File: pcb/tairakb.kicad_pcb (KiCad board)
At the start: 2 copper layers, 144 x 116 mm, 79 parts, among them SW1 SW_Push, SW10 SW_Push, SW11 SW_Push, SW12 SW_Push, SW13 SW_Push, SW14 SW_Push, SW15 SW_Push, SW16 SW_Push, SW17 SW_Push, SW18 SW_Push, SW19 SW_Push, SW2 SW_Push, SW20 SW_Push, SW20-1 SW_Push, SW21 SW_Push, SW22 SW_Push, SW23 SW_Push, SW24 SW_Push, SW25 SW_Push, SW26 SW_Push, SW27 SW_Push, SW28 SW_Push, SW29 SW_Push, SW3 SW_Push, SW30 SW_Push, SW31 SW_Push, SW32 SW_Push, SW33 SW_Push, SW4 SW_Push, SW5 SW_Push, SW6 SW_Push, SW7 SW_Push, SW8 SW_Push, SW9 SW_Push, U3 nice!nano

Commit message: Add traces routed by hand
Previously the diodes were connected from the columns to the switches.
Both the ErgoDash and the Corne have them behind the switches connected
to the rows. Since I positioned the diodes on the PCB like they are in
the ErgoDash and Corne, the routing was much more difficult than intended.

This moves the diodes behind the switches and also moves them around a
bit on the PCB. This allowed me to hand route all traces easily, so this
time no autorouter has been involved.

The via count is rather large (156). I opted to rather have ONE trace
and then interconnect each component with vias itself. An alternative
could be to run traces for rows and columns on both layers, but then
there still would be a lot of conflicting paths requiring vias anyway.

I also removed both GND zones. There is nothing on the board that needs
ground except the nice!nano and the battery and I didn't want to start
adding complicated routing just to get GND zones on the whole board. I
left one GND zone in the nice!nano area since it seems reasonable there.
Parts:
- moved D32 20.9 mm to (199.6, 109.6), turned to 330 degrees
- moved D30 16.6 mm to (196.0, 144.4)
- moved D33 16.6 mm to (211.6, 153.4)
- moved D25 16.6 mm to (180.3, 135.5)
- moved D31 12.0 mm to (198.7, 111.1), turned to 330 degrees
- turned D1 to 270 degrees
- turned D10 to 270 degrees
- turned D11 to 270 degrees
- turned D12 to 270 degrees
- turned D13 to 270 degrees
- turned D14 to 270 degrees
- turned D15 to 270 degrees
- turned D16 to 270 degrees
- turned D17 to 270 degrees
- turned D18 to 270 degrees
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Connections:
- D1 pad 1: Net-(D1-Pad1) -> /row0
- D1 pad 2: /col0 -> Net-(D1-Pad2)
- D10 pad 1: Net-(D10-Pad1) -> /row4
- D10 pad 2: /col1 -> Net-(D10-Pad2)
- D11 pad 1: Net-(D11-Pad1) -> /row0
- D11 pad 2: /col2 -> Net-(D11-Pad2)
- D12 pad 1: Net-(D12-Pad1) -> /row1
- D12 pad 2: /col2 -> Net-(D12-Pad2)
- D13 pad 1: Net-(D13-Pad1) -> /row2
- D13 pad 2: /col2 -> Net-(D13-Pad2)
- D14 pad 1: Net-(D14-Pad1) -> /row3
- D14 pad 2: /col2 -> Net-(D14-Pad2)
- D15 pad 1: Net-(D15-Pad1) -> /row4
- D15 pad 2: /col2 -> Net-(D15-Pad2)
- D16 pad 1: Net-(D16-Pad1) -> /row0
- D16 pad 2: /col3 -> Net-(D16-Pad2)
- D17 pad 1: Net-(D17-Pad1) -> /row1
- D17 pad 2: /col3 -> Net-(D17-Pad2)
- D18 pad 1: Net-(D18-Pad1) -> /row2
- D18 pad 2: /col3 -> Net-(D18-Pad2)
- D19 pad 1: Net-(D19-Pad1) -> /row3
- D19 pad 2: /col3 -> Net-(D19-Pad2)
- D2 pad 1: Net-(D2-Pad1) -> /row1
- D2 pad 2: /col0 -> Net-(D2-Pad2)
- D20 pad 1: Net-(D20-Pad1) -> /row4
- D20 pad 2: /col3 -> Net-(D20-Pad2)
- D21 pad 1: Net-(D21-Pad1) -> /row0
- D21 pad 2: /col4 -> Net-(D21-Pad2)
- D22 pad 1: Net-(D22-Pad1) -> /row1
- D22 pad 2: /col4 -> Net-(D22-Pad2)
- D23 pad 1: Net-(D23-Pad1) -> /row2
- D23 pad 2: /col4 -> Net-(D23-Pad2)
- D24 pad 1: Net-(D24-Pad1) -> /row3
- D24 pad 2: /col4 -> Net-(D24-Pad2)
- D25 pad 1: Net-(D25-Pad1) -> /row4
- D25 pad 2: /col4 -> Net-(D25-Pad2)
- D26 pad 1: Net-(D26-Pad1) -> /row0
- D26 pad 2: /col5 -> Net-(D26-Pad2)
- D27 pad 1: Net-(D27-Pad1) -> /row1
- D27 pad 2: /col5 -> Net-(D27-Pad2)
- D28 pad 1: Net-(D28-Pad1) -> /row2
- D28 pad 2: /col5 -> Net-(D28-Pad2)
- D29 pad 1: Net-(D29-Pad1) -> /row3
- D29 pad 2: /col5 -> Net-(D29-Pad2)
- D3 pad 1: Net-(D3-Pad1) -> /row2
- D3 pad 2: /col0 -> Net-(D3-Pad2)
- D30 pad 1: Net-(D30-Pad1) -> /row4
- D30 pad 2: /col5 -> Net-(D30-Pad2)
- D31 pad 1: Net-(D31-Pad1) -> /row2
- D31 pad 2: /col6 -> Net-(D31-Pad2)
- D32 pad 1: Net-(D32-Pad1) -> /row3
- D32 pad 2: /col6 -> Net-(D32-Pad2)
- D33 pad 1: Net-(D33-Pad1) -> /row4
- D33 pad 2: /col6 -> Net-(D33-Pad2)
- D4 pad 1: Net-(D4-Pad1) -> /row3
- D4 pad 2: /col0 -> Net-(D4-Pad2)
- D5 pad 1: Net-(D5-Pad1) -> /row4
- D5 pad 2: /col0 -> Net-(D5-Pad2)
- D6 pad 1: Net-(D6-Pad1) -> /row0
- D6 pad 2: /col1 -> Net-(D6-Pad2)
- D7 pad 1: Net-(D7-Pad1) -> /row1
- D7 pad 2: /col1 -> Net-(D7-Pad2)
- D8 pad 1: Net-(D8-Pad1) -> /row2
- D8 pad 2: /col1 -> Net-(D8-Pad2)
- D9 pad 1: Net-(D9-Pad1) -> /row3
- D9 pad 2: /col1 -> Net-(D9-Pad2)
- SW1 pad 1: /row0 -> Net-(D1-Pad2)
- SW1 pad 2: Net-(D1-Pad1) -> /col0
- SW10 pad 1: /row4 -> Net-(D10-Pad2)
- SW10 pad 2: Net-(D10-Pad1) -> /col1
- SW11 pad 1: /row0 -> Net-(D11-Pad2)
- SW11 pad 2: Net-(D11-Pad1) -> /col2
- SW12 pad 1: /row1 -> Net-(D12-Pad2)
- SW12 pad 2: Net-(D12-Pad1) -> /col2
- SW13 pad 1: /row2 -> Net-(D13-Pad2)
- SW13 pad 2: Net-(D13-Pad1) -> /col2
- SW14 pad 1: /row3 -> Net-(D14-Pad2)
- SW14 pad 2: Net-(D14-Pad1) -> /col2
- SW15 pad 1: /row4 -> Net-(D15-Pad2)
- SW15 pad 2: Net-(D15-Pad1) -> /col2
- SW16 pad 1: /row0 -> Net-(D16-Pad2)
- SW16 pad 2: Net-(D16-Pad1) -> /col3
- SW17 pad 1: /row1 -> Net-(D17-Pad2)
- SW17 pad 2: Net-(D17-Pad1) -> /col3
- SW18 pad 1: /row2 -> Net-(D18-Pad2)
- SW18 pad 2: Net-(D18-Pad1) -> /col3
- SW19 pad 1: /row3 -> Net-(D19-Pad2)
- SW19 pad 2: Net-(D19-Pad1) -> /col3
- SW2 pad 1: /row1 -> Net-(D2-Pad2)
- SW2 pad 2: Net-(D2-Pad1) -> /col0
- SW20 pad 1: /row4 -> Net-(D20-Pad2)
- SW20 pad 2: Net-(D20-Pad1) -> /col3
- SW20-1 pad 1: /row4 -> Net-(D20-Pad2)
- SW20-1 pad 2: Net-(D20-Pad1) -> /col3
- SW21 pad 1: /row0 -> Net-(D21-Pad2)
- SW21 pad 2: Net-(D21-Pad1) -> /col4
- SW22 pad 1: /row1 -> Net-(D22-Pad2)
- SW22 pad 2: Net-(D22-Pad1) -> /col4
- SW23 pad 1: /row2 -> Net-(D23-Pad2)
- SW23 pad 2: Net-(D23-Pad1) -> /col4
- SW24 pad 1: /row3 -> Net-(D24-Pad2)
- SW24 pad 2: Net-(D24-Pad1) -> /col4
- SW25 pad 1: /row4 -> Net-(D25-Pad2)
- SW25 pad 2: Net-(D25-Pad1) -> /col4
- SW26 pad 1: /row0 -> Net-(D26-Pad2)
- SW26 pad 2: Net-(D26-Pad1) -> /col5
- SW27 pad 1: /row1 -> Net-(D27-Pad2)
- SW27 pad 2: Net-(D27-Pad1) -> /col5
- SW28 pad 1: /row2 -> Net-(D28-Pad2)
- SW28 pad 2: Net-(D28-Pad1) -> /col5
- SW29 pad 1: /row3 -> Net-(D29-Pad2)
- SW29 pad 2: Net-(D29-Pad1) -> /col5
- SW3 pad 1: /row2 -> Net-(D3-Pad2)
- SW3 pad 2: Net-(D3-Pad1) -> /col0
- SW30 pad 1: /row4 -> Net-(D30-Pad2)
- SW30 pad 2: Net-(D30-Pad1) -> /col5
- SW31 pad 1: /row2 -> Net-(D31-Pad2)
- SW31 pad 2: Net-(D31-Pad1) -> /col6
- SW32 pad 1: /row3 -> Net-(D32-Pad2)
- SW32 pad 2: Net-(D32-Pad1) -> /col6
- SW33 pad 1: /row4 -> Net-(D33-Pad2)
- SW33 pad 2: Net-(D33-Pad1) -> /col6
- SW4 pad 1: /row3 -> Net-(D4-Pad2)
- SW4 pad 2: Net-(D4-Pad1) -> /col0
- SW5 pad 1: /row4 -> Net-(D5-Pad2)
- SW5 pad 2: Net-(D5-Pad1) -> /col0
- SW6 pad 1: /row0 -> Net-(D6-Pad2)
- SW6 pad 2: Net-(D6-Pad1) -> /col1
- SW7 pad 1: /row1 -> Net-(D7-Pad2)
- SW7 pad 2: Net-(D7-Pad1) -> /col1
- SW8 pad 1: /row2 -> Net-(D8-Pad2)
- SW8 pad 2: Net-(D8-Pad1) -> /col1
- SW9 pad 1: /row3 -> Net-(D9-Pad2)
- SW9 pad 2: Net-(D9-Pad1) -> /col1
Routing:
- net /row3: track 280.8 -> 157.8 mm, vias 6 -> 12
- net /row2: track 280.0 -> 159.6 mm, vias 6 -> 11
- net /row0: track 251.0 -> 152.4 mm, vias 3 -> 8
- net /row1: track 207.3 -> 138.3 mm, vias 5 -> 8
- net /row4: track 315.9 -> 254.2 mm, vias 4 -> 7
- net Net-(D20-Pad1): track 53.2 -> 0.00 mm, vias 1 -> 0
- net Net-(D20-Pad2): track 0.00 -> 51.1 mm, vias 0 -> 3
- net /col2: track 173.0 -> 222.5 mm, vias 6 -> 5
- net /col3: track 168.4 -> 217.4 mm, vias 3 -> 6
- net Net-(D32-Pad2): track 0.00 -> 38.4 mm, vias 0 -> 2
- net Net-(D31-Pad1): track 36.7 -> 0.00 mm, vias 1 -> 0
- net Net-(D19-Pad1): track 34.4 -> 0.00 mm, vias 1 -> 0
- net Net-(D21-Pad1): track 31.2 -> 0.00 mm, vias 1 -> 0
- net Net-(D33-Pad1): track 30.8 -> 0.00 mm, vias 1 -> 0
- net Net-(D32-Pad1): track 30.1 -> 0.00 mm, vias 1 -> 0
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- removed copper zone on F.Cu, net GND

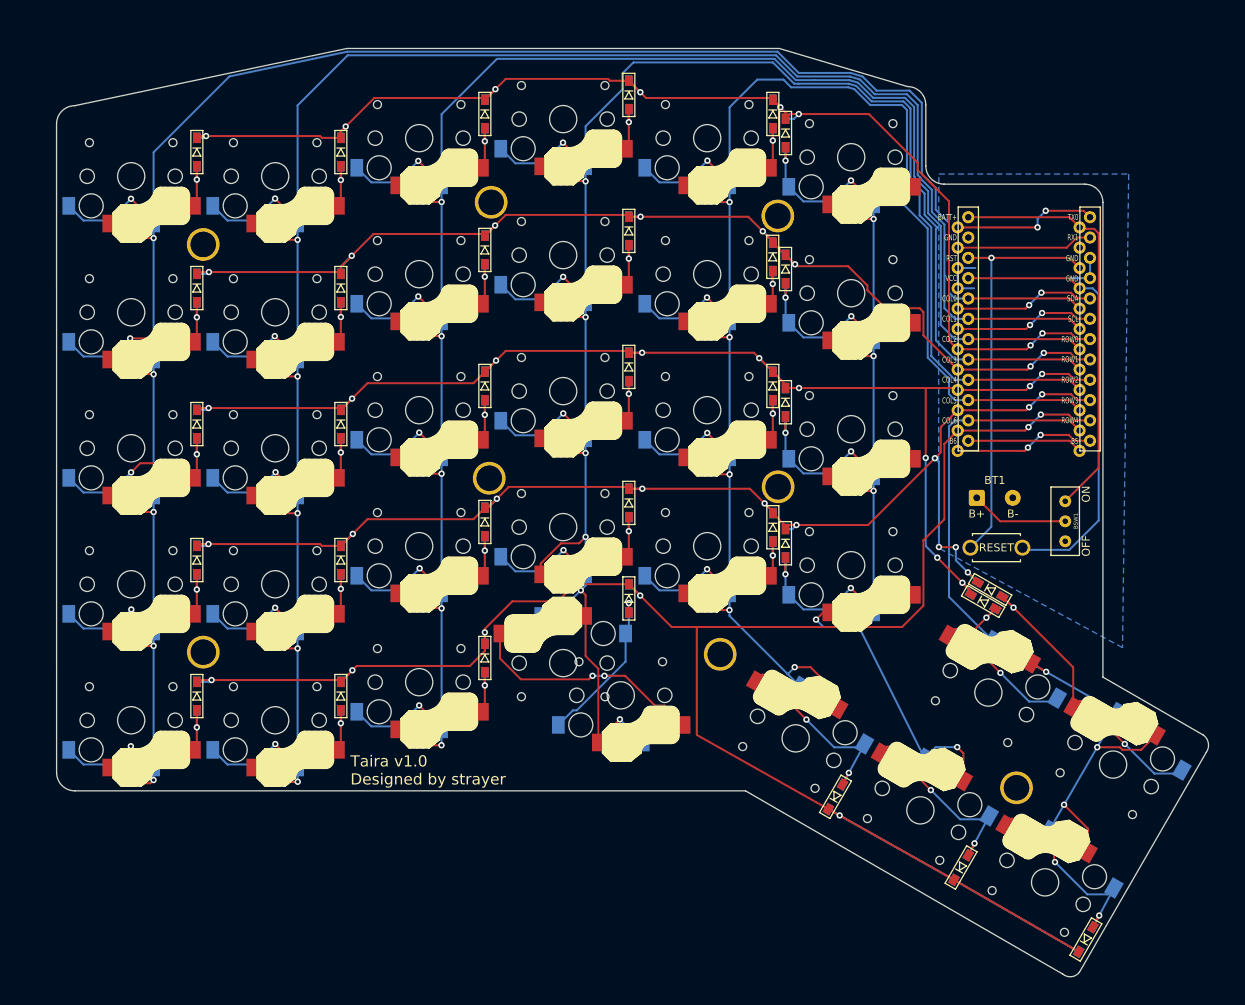
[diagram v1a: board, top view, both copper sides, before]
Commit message: Add revision 1.0
Pretty much everything changed. A lot of things were fixed, plates were
added and the spacing between the keys is now 1mm (there was no spacing
before).
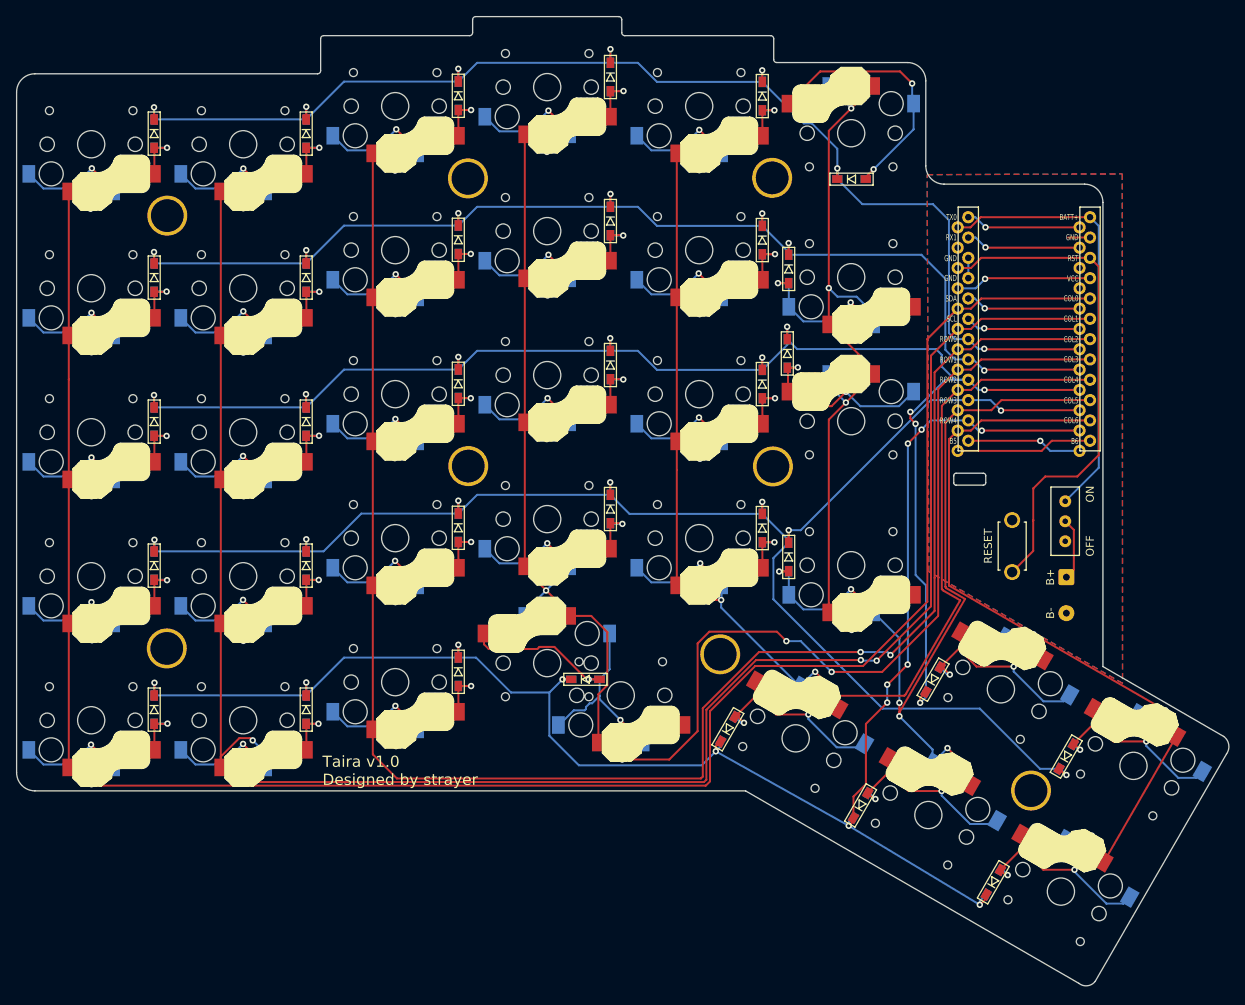
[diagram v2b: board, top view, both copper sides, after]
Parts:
- D1, D10, D11, D12, D13, D14, D15, D16, D17, D18, D19, D2, D20, D21, D22, D23, D24, D25, D26, D27, D28, D29, D3, D30, D31, D32, D33, D4, D5, D6, D7, D8, D9: footprint kbd:D3_SMD -> tairakb:D3_SMD
- RSW1: footprint kbd:ResetSW -> tairakb:ResetSW
- moved D32 23.0 mm to (209.1, 130.5), turned to 60 degrees
- moved D25 15.9 mm to (166.8, 127.1)
- moved BT1 15.0 mm to (209.1, 108.1), turned to 270 degrees
- moved D30 14.8 mm to (183.4, 136.6)
- moved D33 13.6 mm to (200.0, 146.2)
- moved D31 11.6 mm to (192.5, 120.9), turned to 60 degrees
- moved D20 11.5 mm to (149.0, 120.9), turned to 0 degrees
- moved D26 10.1 mm to (182.3, 58.3), turned to 0 degrees
- moved SW1 6.40 mm to (87.2, 54.0)
- moved D28 6.10 mm to (174.3, 80.1)
- moved SW2 5.83 mm to (87.2, 72.0)
- moved D1 5.81 mm to (95.1, 52.6)
- moved H1 5.76 mm to (96.8, 62.9)
- moved SW6 5.66 mm to (106.2, 54.0)
- moved D5 5.59 mm to (95.1, 124.6)
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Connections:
- BSW1 pad 1: Net-(BSW1-Pad1) -> (no net)
- RSW1 pad 1: VCC -> GND
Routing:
- net /row3: track 157.8 -> 201.9 mm, vias 12 -> 8
- net VCC: track 56.6 -> 17.1 mm, vias 0 -> 1
- net /row4: track 254.2 -> 215.7 mm, vias 7 -> 13
- net /col5: track 154.9 -> 188.1 mm, vias 5 -> 7
- net /row2: track 159.6 -> 192.1 mm, vias 11 -> 10
- net /col0: track 255.7 -> 283.2 mm
- net /col2: track 222.5 -> 248.3 mm, vias 5 -> 7
- net /col1: track 244.2 -> 269.1 mm, vias 5 -> 7
- net /col4: track 189.1 -> 175.1 mm
- net /row1: track 138.3 -> 151.0 mm, vias 8 -> 7
- net /RST: track 51.8 -> 63.6 mm, vias 1 -> 0
- net Net-(D32-Pad2): track 38.4 -> 26.6 mm
- net /row0: track 152.4 -> 162.3 mm, vias 8 -> 7
- net /col3: track 217.4 -> 226.8 mm, vias 6 -> 7
- net /col6: track 100.3 -> 108.9 mm
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- added copper zone on F.Cu, net GND
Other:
- board size 144 x 116 mm -> 151.5 x 121.2 mm
